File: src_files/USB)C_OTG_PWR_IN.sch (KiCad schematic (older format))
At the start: 19 parts, among them J10 Conn_01x02_Male, J11 USB_C_Receptacle

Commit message: updated footprint and schematics
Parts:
- removed J10: Conn_01x02_Male, Connector_Phoenix_MC:PhoenixContact_MC_1,5_2-G-3.81_1x02_P3.81mm_Horizontal, symbol Connector:Conn_01x02_Male
- added TP18: PWR_IN+, TestPoint:TestPoint_Pad_2.0x2.0mm, symbol Connector:TestPoint
- added TP19: PWR_IN-, TestPoint:TestPoint_Pad_2.0x2.0mm, symbol Connector:TestPoint
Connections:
- net GND: now also TP19.1
- net VBUS: now also TP18.1
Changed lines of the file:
@@
 $Descr A4 11693 8268
 encoding utf-8
-Sheet 14 15
+Sheet 13 16
 Title ""
 Date ""
@@
 Text HLabel 5875 2375 2    50   Input ~ 0
 USB_OTG0_VBUSDET
-$Comp
-L Connector:Conn_01x02_Male J10
-U 1 1 6A39320C
-P 1100 4950
-F 0 "J10" H 1208 5131 50  0000 C CNN
-F 1 "Conn_01x02_Male" H 1208 5040 50  0000 C CNN
-F 2 "Connector_Phoenix_MC:PhoenixContact_MC_1,5_2-G-3.81_1x02_P3.81mm_Horizontal" H 1100 4950 50  0001 C CNN
-F 3 "~" H 1100 4950 50  0001 C CNN
-	1    1100 4950
-	1    0    0    -1
-$EndComp
 Wire Wire Line
 	1300 4950 1825 4950
@@
 L OLIMEX_Power:GND #PWR?
 U 1 1 6A394CB4
-P 1800 5175
+P 1800 5300
 AR Path="/6A394CB4" Ref="#PWR?"  Part="1"
 AR Path="/6823D52E/6A394CB4" Ref="#PWR0267"  Part="1"
-F 0 "#PWR0267" H 1800 4925 50  0001 C CNN
-F 1 "GND" H 1805 5002 50  0000 C CNN
-F 2 "" H 1800 5175 60  0000 C CNN
-F 3 "" H 1800 5175 60  0000 C CNN
-	1    1800 5175
-	1    0    0    -1
-$EndComp
-Wire Wire Line
-	1300 5050 1800 5050
-Wire Wire Line
-	1800 5050 1800 5175
+F 0 "#PWR0267" H 1800 5050 50  0001 C CNN
+F 1 "GND" H 1805 5127 50  0000 C CNN
+F 2 "" H 1800 5300 60  0000 C CNN
+F 3 "" H 1800 5300 60  0000 C CNN
+	1    1800 5300
+	1    0    0    -1
+$EndComp
+Wire Wire Line
+	1300 5175 1800 5175
+Wire Wire Line
+	1800 5175 1800 5300
 Text Label 1825 4950 0    39   ~ 0
 POWER_IN_CONN
@@
 Wire Wire Line
 	7050 900  7275 900
+$Comp
+L Connector:TestPoint TP?
+U 1 1 62F91836
+P 1300 4950
+AR Path="/672F9255/62F91836" Ref="TP?"  Part="1"
+AR Path="/6823D52E/62F91836" Ref="TP18"  Part="1"
+F 0 "TP18" V 1254 5138 50  0000 L CNN
+F 1 "PWR_IN+" V 1345 5138 50  0000 L CNN
+F 2 "TestPoint:TestPoint_Pad_2.0x2.0mm" H 1500 4950 50  0001 C CNN
+F 3 "~" H 1500 4950 50  0001 C CNN
+	1    1300 4950
+	0    -1   -1   0
+$EndComp
+$Comp
+L Connector:TestPoint TP?
+U 1 1 62F9183C
+P 1300 5175
+AR Path="/672F9255/62F9183C" Ref="TP?"  Part="1"
+AR Path="/6823D52E/62F9183C" Ref="TP19"  Part="1"
+F 0 "TP19" V 1254 5363 50  0000 L CNN
+F 1 "PWR_IN-" V 1345 5363 50  0000 L CNN
+F 2 "TestPoint:TestPoint_Pad_2.0x2.0mm" H 1500 5175 50  0001 C CNN
+F 3 "~" H 1500 5175 50  0001 C CNN
+	1    1300 5175
+	0    -1   -1   0
+$EndComp
 $EndSCHEMATC

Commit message: wireless power TX RX added
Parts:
- removed D24: ESD5451R-2/TR, greencharge-footprints:DFP1006-2L, symbol Device:D_TVS
- removed F1: mSMD300, Fuse:Fuse_1812_4532Metric, symbol OLIMEX_Devices:FUSE
- removed J11: USB_C_Receptacle, greencharge-footprints:GCT_USB4056-03-A_REVA, symbol Connector:USB_C_Receptacle
- added C298, C306, C307: 10uF, Capacitor_SMD:C_0402_1005Metric, symbol Device:C_Small
- added C299: 4.7nF, Capacitor_SMD:C_0402_1005Metric, symbol Device:C_Small
- added C300, C301: 22nF, Capacitor_SMD:C_01005_0402Metric, symbol Device:C_Small
- added C302, C303, C304, C305, C313: 47nF, Capacitor_SMD:C_01005_0402Metric, symbol Device:C_Small
- added C308, C309: 2.2uF, Capacitor_SMD:C_0603_1608Metric, symbol Device:C_Small
- added C310, C311, C312: 10uF, Capacitor_SMD:C_0603_1608Metric, symbol Device:C_Small
- added C314, C315, C316: 100nF, Capacitor_SMD:C_01005_0402Metric, symbol Device:C_Small
- added C317: 15uF, Capacitor_SMD:C_0805_2012Metric, symbol Device:C_Small
- added C318, C319: 100nF, Capacitor_SMD:C_0402_1005Metric, symbol Device:C_Small
- added C320: 100pF, Capacitor_SMD:C_0402_1005Metric, symbol Device:C_Small
- added D4: LED, LED_SMD:LED_0603_1608Metric, symbol Device:LED
- added D5, D6: SMAJ16A, Diode_SMD:D_SMA, symbol dk_TVS-Diodes:ESD5Z3_3T1G
- added L16: MWSA1004S-3R3MT, greencharge-footprints:MWSA1004S-3R3MT, symbol OLIMEX_RCL:INDUCTOR_SMALL
- added R66, R67: 470R, Resistor_SMD:R_0402_1005Metric, symbol Device:R_US
- added R68, R69, R70: 47K, Resistor_SMD:R_0402_1005Metric, symbol Device:R_US
- added TP22: RX_COIL+, TestPoint:TestPoint_Pad_1.5x1.5mm, symbol Connector:TestPoint
- added TP23: rx_vout, TestPoint:TestPoint_Pad_2.0x2.0mm, symbol Connector:TestPoint
- added TP24: USB_D-, TestPoint:TestPoint_Pad_1.0x1.0mm, symbol Connector:TestPoint
- added TP25: USB_D+, TestPoint:TestPoint_Pad_1.0x1.0mm, symbol Connector:TestPoint
- added U13: STWLC68, greencharge-footprints:STWLC68, symbol GCL_Integrated-Circuits:STWLC68
- added U14: TPS56637RPAR, greencharge-footprints:TPS56637RPAR, symbol GCL_Integrated-Circuits:TPS56637RPAR
- R93: value 5.1K -> 100K
- R94: value 5.1K -> 20K
- R95: value 2.2R -> 73.2K
- R96: value 2.2R -> 10K
- TP16: value VBUS -> 5V_VIN
- TP17: value 5V -> RX_COIL-; footprint TestPoint:TestPoint_Pad_D1.0mm -> TestPoint:TestPoint_Pad_1.5x1.5mm
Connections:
- net +5V: now also R93.1, R94.1, R95.1, TP18.1, L16.2; no longer TP17.1
- net GND: now also R96.2, C298.2, C306.2, C307.2, C308.2, C309.2, C310.2, C311.2, C312.2, C317.2, C318.2, D5.A, D6.A, U13.A1 (VSSP), U13.A8 (VSSP), U13.B1 (VSSP), U13.B8 (VSSP), U13.C4 (VSSA), U13.C5 (VSSA), U13.D3 (VSSA), U13.D4 (VSSA), U13.E4 (VSSD), U13.E5 (VSSA), U13.F3 (VSSD), U13.F4 (VSSD), U13.F5 (VSSA), U13.F6 (VSSA), U13.G1 (DFT), U13.G2 (VSSD), U13.G3 (VSSD), U13.G4 (VSSD), U13.G6 (VSSA), U13.G7 (VSSA), U13.H3 (VSSD), U13.H4 (VSSD), U13.H5 (VSSD), U13.H6 (VSSD), U13.H7 (VSSD), U13.J5 (BOOT_SEL), U14.10 (MODE), U14.3 (AGND), U14.9 (PGND); no longer R93.1, R94.1
- net USB_OTG0_D+: now also TP25.1; no longer R96.1
- net USB_OTG0_D-: now also TP24.1; no longer R95.1
- net VBUS: no longer TP18.1
- net at R93.2: now also U14.4 (PG)
- net at R94.2: now also C320.2
- net at R95.2: now also R96.1, C320.1, U14.2 (FB)
- new net: C298.1, C299.2, C306.1, C307.1, R66.2, U13.A4 (VRECT), U13.A5 (VRECT), U13.B4 (VRECT), U13.B5 (VRECT), U13.C3 (VRECT)
- new net: C300.1, C302.1, C303.1, C313.2, C314.2, C315.2, C316.2, D5.K, U13.A6 (AC1), U13.A7 (AC1), U13.B6 (AC1), U13.B7 (AC1)
- new net: C304.2, U13.C1 (BOOT2)
- new net: R66.1, U13.C2 (IEXT)
- new net: U13.C6 (NC), U13.D6 (NC)
- new net: C305.2, U13.C7 (CLAMP2)
- new net: C302.2, U13.C8 (CLAMP1)
- new net: C301.2, U13.D7 (COMM2)
- new net: C300.2, U13.D8 (COMM1)
- new net: C308.1, U13.E6 (V5V0), U13.F7 (V5V0)
- new net: C303.2, U13.E7 (BOOT1)
- new net: C299.1, U13.E8 (BOOT)
- new net: D4.1 (K), U13.H2 (GPIO0)
- new net: R69.2, U13.H8 (SCL)
- new net: R68.2, U13.J7 (INTB)
- new net: R70.2, U13.J8 (SDA)
- new net: D4.2 (A), R67.2
- new net: C319.2, L16.1, U14.6 (SW)
- new net: C319.1, U14.7 (BOOT)
- new net COIL+: C313.1, C314.1, C315.1, C316.1, TP22.1
- new net COIL-: C301.1, C304.1, C305.1, D6.K, TP17.1, U13.A2 (AC2), U13.A3 (AC2), U13.B2 (AC2), U13.B3 (AC2)
- new net RX_VOUT: C310.1, C311.1, C312.1, C317.1, C318.1, TP23.1, U13.D2 (VOUT), U13.E1 (VOUT), U13.E2 (VOUT), U13.E3 (VOUT), U13.F2 (VOUT), U14.1 (EN), U14.11 (VIN_2), U14.12 (VIN_3), U14.13 (VIN_4), U14.8 (VIN_1)
- new net v1v8: C309.1, R67.1, R68.1, R69.1, R70.1, U13.G5 (V1V8), U13.G8 (V1V8), U13.J6 (RSTB)
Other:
- note added: "5V 6A BUCK"
- note added: "FILTER"
- note added: "MAIN SYSTEM SUPPLY RAIL\n5V / 6A"
- note added: "OPTIONAL POWER INPUT 5V >2A"
- note added: "PROGRAMABLE OUTPUT OF THE \nRECEIVER LDO RANGE 2.5W-20W. \nso MAX OUT= 20V at 1A."
- note added: "WIRELESS POWER RECEIVER"
- note added: "base on selection\nto achieve 100KHz resonance\nL=7.3uH C=350nF"
- note added: "coil type A5\nhttps://kimchen8.en.made-in-china.com/product/uBcmjaAlYKht/China-Square-Rx-Coil-Antenna-Coil-for-Samsung-Charging-Receiver.html"
- note added: "to filter out V_spikes"
- moved on the sheet: C254, C255, C256, C257, C258, D23, D25, R97, R98, TP16, TP18, TP19

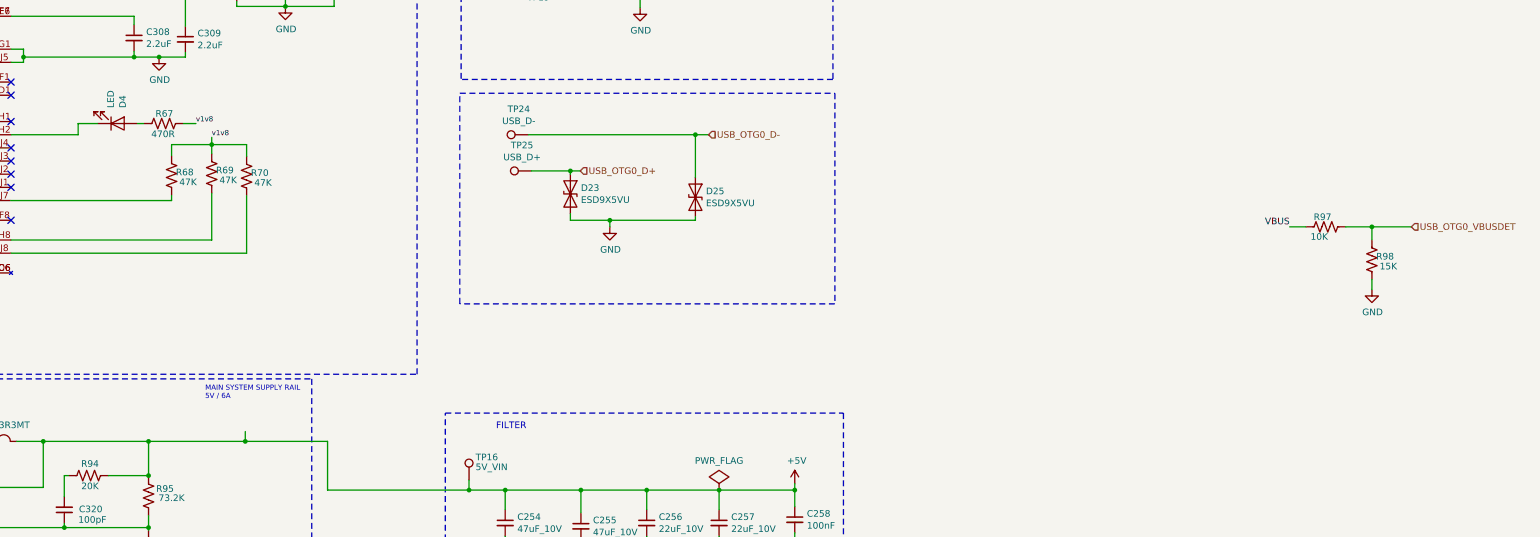
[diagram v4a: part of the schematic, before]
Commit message: updates rules check and associations
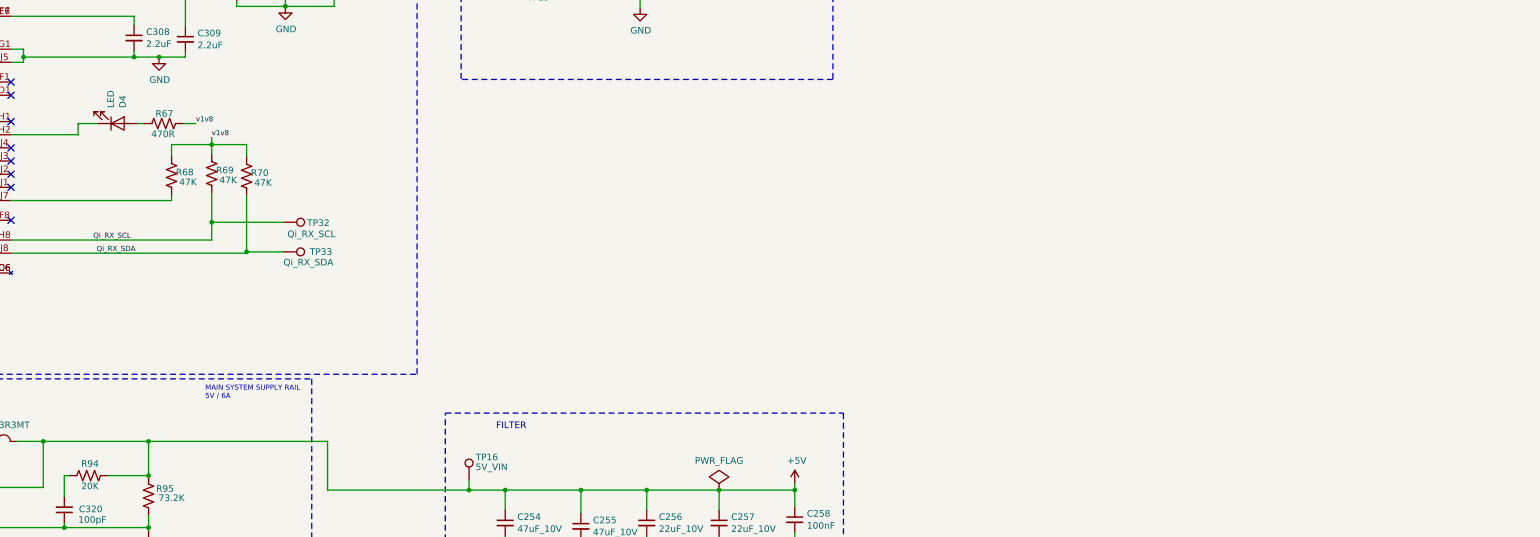
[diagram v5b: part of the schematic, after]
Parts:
- removed D23, D25: ESD9X5VU, greencharge-footprints:ESD9X5VU_DFN1006-2, symbol Device:D_TVS
- removed R97: 10K, Resistor_SMD:R_0402_1005Metric, symbol Device:R_US
- removed R98: 15K, Resistor_SMD:R_0402_1005Metric, symbol Device:R_US
- removed TP24: USB_D-, TestPoint:TestPoint_Pad_1.0x1.0mm, symbol Connector:TestPoint
- removed TP25: USB_D+, TestPoint:TestPoint_Pad_1.0x1.0mm, symbol Connector:TestPoint
- added TP32: Qi_RX_SCL, TestPoint:TestPoint_Pad_D1.0mm, symbol Connector:TestPoint
- added TP33: Qi_RX_SDA, TestPoint:TestPoint_Pad_D1.0mm, symbol Connector:TestPoint
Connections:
- net Qi_RX_SCL: now reaches R69.2, U13.H8 (SCL)
- net Qi_RX_SCL: now also TP32.1
- net Qi_RX_SDA: now reaches R70.2, U13.J8 (SDA)
- net Qi_RX_SDA: now also TP33.1
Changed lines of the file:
@@
 $Descr A4 11693 8268
 encoding utf-8
-Sheet 11 17
+Sheet 17 17
 Title ""
 Date ""
@@
 $EndDescr
 $Comp
-L Device:D_TVS D?
-U 1 1 682BBBF7
-P 8990 2755
-AR Path="/61C73AB6/682BBBF7" Ref="D?"  Part="1"
-AR Path="/682BBBF7" Ref="D?"  Part="1"
-AR Path="/6823D52E/682BBBF7" Ref="D23"  Part="1"
-F 0 "D23" V 8944 2835 50  0000 L CNN
-F 1 "ESD9X5VU" V 9035 2835 50  0000 L CNN
-F 2 "greencharge-footprints:ESD9X5VU_DFN1006-2" H 8990 2755 50  0001 C CNN
-F 3 "~" H 8990 2755 50  0001 C CNN
-	1    8990 2755
-	0    1    1    0
-$EndComp
-$Comp
 L Device:C_Small C?
 U 1 1 682BBC5C
@@
 	1    0    0    -1
 $EndComp
-$Comp
-L OLIMEX_Power:GND #PWR?
-U 1 1 682BBC7A
-P 9290 3005
-AR Path="/682BBC7A" Ref="#PWR?"  Part="1"
-AR Path="/6823D52E/682BBC7A" Ref="#PWR0271"  Part="1"
-F 0 "#PWR0271" H 9290 2755 50  0001 C CNN
-F 1 "GND" H 9295 2832 50  0000 C CNN
-F 2 "" H 9290 3005 60  0000 C CNN
-F 3 "" H 9290 3005 60  0000 C CNN
-	1    9290 3005
-	1    0    0    -1
-$EndComp
-Wire Wire Line
-	8990 2905 8990 2955
-Wire Wire Line
-	8990 2955 9290 2955
-Wire Wire Line
-	9290 2955 9290 3005
-Connection ~ 9290 2955
 Wire Wire Line
 	10695 5005 10695 5130
@@
 Wire Wire Line
 	9520 1215 9520 1340
-Wire Wire Line
-	8990 2580 8990 2605
-Text HLabel 9065 2580 2    50   Input ~ 0
-USB_OTG0_D+
-Text HLabel 10040 2305 2    50   Input ~ 0
-USB_OTG0_D-
-Wire Wire Line
-	9940 2955 9940 2930
-Wire Wire Line
-	9290 2955 9940 2955
-$Comp
-L Device:D_TVS D?
-U 1 1 682BBC24
-P 9940 2780
-AR Path="/61C73AB6/682BBC24" Ref="D?"  Part="1"
-AR Path="/682BBC24" Ref="D?"  Part="1"
-AR Path="/6823D52E/682BBC24" Ref="D25"  Part="1"
-F 0 "D25" V 9894 2860 50  0000 L CNN
-F 1 "ESD9X5VU" V 9985 2860 50  0000 L CNN
-F 2 "greencharge-footprints:ESD9X5VU_DFN1006-2" H 9940 2780 50  0001 C CNN
-F 3 "~" H 9940 2780 50  0001 C CNN
-	1    9940 2780
-	0    1    1    0
-$EndComp
-Wire Wire Line
-	9065 2580 8990 2580
-Wire Wire Line
-	10040 2305 9940 2305
 $Comp
 L OLIMEX_Power:PWR_FLAG #FLG0101
@@
 	4740 3105 6265 3105
 Wire Wire Line
-	6265 3105 6265 2750
-Wire Wire Line
-	4740 3205 6530 3205
-Wire Wire Line
-	6530 3205 6530 2770
+	6265 3105 6265 2970
 Wire Wire Line
 	4740 2805 5960 2805
@@
 	1    0    0    -1
 $EndComp
-$Comp
-L Connector:TestPoint TP24
-U 1 1 622DC098
-P 8670 2305
-F 0 "TP24" V 8865 2377 50  0000 C CNN
-F 1 "USB_D-" V 8774 2377 50  0000 C CNN
-F 2 "TestPoint:TestPoint_Pad_1.0x1.0mm" H 8870 2305 50  0001 C CNN
-F 3 "~" H 8870 2305 50  0001 C CNN
-	1    8670 2305
-	0    -1   -1   0
-$EndComp
-$Comp
-L Connector:TestPoint TP25
-U 1 1 6230EBE6
-P 8695 2580
-F 0 "TP25" V 8890 2652 50  0000 C CNN
-F 1 "USB_D+" V 8799 2652 50  0000 C CNN
-F 2 "TestPoint:TestPoint_Pad_1.0x1.0mm" H 8895 2580 50  0001 C CNN
-F 3 "~" H 8895 2580 50  0001 C CNN
-	1    8695 2580
-	0    -1   -1   0
-$EndComp
-Wire Wire Line
-	8990 2580 8695 2580
-Connection ~ 8990 2580
-Wire Wire Line
-	8670 2305 9940 2305
-Connection ~ 9940 2305
-Wire Wire Line
-	9940 2305 9940 2630
-Text Label 14455 3005 2    50   ~ 0
-VBUS
-Wire Wire Line
-	14455 3005 14580 3005
-$Comp
-L OLIMEX_Power:GND #PWR?
-U 1 1 682BBC41
-P 15080 3480
-AR Path="/682BBC41" Ref="#PWR?"  Part="1"
-AR Path="/6823D52E/682BBC41" Ref="#PWR0272"  Part="1"
-F 0 "#PWR0272" H 15080 3230 50  0001 C CNN
-F 1 "GND" H 15085 3307 50  0000 C CNN
-F 2 "" H 15080 3480 60  0000 C CNN
-F 3 "" H 15080 3480 60  0000 C CNN
-	1    15080 3480
-	1    0    0    -1
-$EndComp
-Text HLabel 15380 3005 2    50   Input ~ 0
-USB_OTG0_VBUSDET
-Wire Wire Line
-	15080 3480 15080 3405
-Wire Wire Line
-	15080 3005 15380 3005
-Wire Wire Line
-	14880 3005 15080 3005
-Connection ~ 15080 3005
-Wire Wire Line
-	15080 3005 15080 3105
-$Comp
-L Device:R_US R?
-U 1 1 682BBC37
-P 15080 3255
-AR Path="/682BBC37" Ref="R?"  Part="1"
-AR Path="/6823D52E/682BBC37" Ref="R98"  Part="1"
-F 0 "R98" H 15180 3280 50  0000 C CNN
-F 1 "15K" H 15205 3205 50  0000 C CNN
-F 2 "Resistor_SMD:R_0402_1005Metric" V 15120 3245 50  0001 C CNN
-F 3 "~" H 15080 3255 50  0001 C CNN
-	1    15080 3255
-	1    0    0    -1
-$EndComp
-$Comp
-L Device:R_US R?
-U 1 1 682BBC31
-P 14730 3005
-AR Path="/682BBC31" Ref="R?"  Part="1"
-AR Path="/6823D52E/682BBC31" Ref="R97"  Part="1"
-F 0 "R97" V 14655 2980 50  0000 C CNN
-F 1 "10K" V 14805 2955 50  0000 C CNN
-F 2 "Resistor_SMD:R_0402_1005Metric" V 14770 2995 50  0001 C CNN
-F 3 "~" H 14730 3005 50  0001 C CNN
-	1    14730 3005
-	0    1    1    0
-$EndComp
 Text Notes 6295 875  0    39   ~ 0
 PROGRAMABLE OUTPUT OF THE \nRECEIVER LDO RANGE 2.5W-20W. \nso MAX OUT= 20V at 1A.
@@
 Connection ~ 5145 5290
 Connection ~ 5785 4635
-Wire Wire Line
-	6520 4560 6520 4635
 Text Notes 6215 4320 0    39   ~ 0
 MAIN SYSTEM SUPPLY RAIL\n5V / 6A
@@
 Wire Wire Line
 	7145 5005 8220 5005
-Wire Wire Line
-	5785 4635 6520 4635
-Connection ~ 6520 4635
-Wire Wire Line
-	6520 4635 7145 4635
 Connection ~ 8220 5005
 Wire Wire Line
@@
 	8040 4420 11065 4420
 Wire Notes Line
-	11000 1990 11000 3590
-Wire Notes Line
-	11000 3590 8150 3590
-Wire Notes Line
-	8150 3590 8150 1990
-Wire Notes Line
-	8150 1990 11000 1990
-Wire Notes Line
 	8165 595  10985 595
 Wire Notes Line
@@
 Wire Wire Line
 	9020 990  9545 990
+Wire Wire Line
+	5785 4635 7145 4635
+Text Label 5365 3105 0    39   ~ 0
+Qi_RX_SCL
+Text Label 5390 3205 0    39   ~ 0
+Qi_RX_SDA
+$Comp
+L Connector:TestPoint TP?
+U 1 1 640203A8
+P 6810 2970
+AR Path="/61C73AB6/640203A8" Ref="TP?"  Part="1"
+AR Path="/62F6D336/640203A8" Ref="TP?"  Part="1"
+AR Path="/6823D52E/640203A8" Ref="TP32"  Part="1"
+F 0 "TP32" V 6815 3150 50  0000 L CNN
+F 1 "Qi_RX_SCL" V 6900 3000 50  0000 L CNN
+F 2 "TestPoint:TestPoint_Pad_D1.0mm" H 7010 2970 50  0001 C CNN
+F 3 "~" H 7010 2970 50  0001 C CNN
+	1    6810 2970
+	0    1    1    0
+$EndComp
+Wire Wire Line
+	4740 3205 6530 3205
+Connection ~ 6530 3195
+Wire Wire Line
+	6530 3195 6530 2770
+Wire Wire Line
+	6530 3205 6530 3195
+Wire Wire Line
+	6810 3195 6530 3195
+$Comp
+L Connector:TestPoint TP?
+U 1 1 6403E2AC
+P 6810 3195
+AR Path="/61C73AB6/6403E2AC" Ref="TP?"  Part="1"
+AR Path="/62F6D336/6403E2AC" Ref="TP?"  Part="1"
+AR Path="/6823D52E/6403E2AC" Ref="TP33"  Part="1"
+F 0 "TP33" V 6810 3395 50  0000 L CNN
+F 1 "Qi_RX_SDA" V 6890 3195 50  0000 L CNN
+F 2 "TestPoint:TestPoint_Pad_D1.0mm" H 7010 3195 50  0001 C CNN
+F 3 "~" H 7010 3195 50  0001 C CNN
+	1    6810 3195
+	0    1    1    0
+$EndComp
+Wire Wire Line
+	6810 2970 6265 2970
+Connection ~ 6265 2970
+Wire Wire Line
+	6265 2970 6265 2750
 $EndSCHEMATC

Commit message: layout change
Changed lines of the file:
@@
 AR Path="/626A6204/62FDE5CD" Ref="TP?"  Part="1"
 AR Path="/6823D52E/62FDE5CD" Ref="TP22"  Part="1"
-F 0 "TP22" V 869 1858 50  0000 L CNN
+F 0 "TP22" V 860 1820 50  0000 L CNN
 F 1 "RX_COIL+" V 995 1610 50  0000 L CNN
 F 2 "TestPoint:TestPoint_Pad_1.5x1.5mm" H 1115 1670 50  0001 C CNN
@@
 AR Path="/626A6204/62FDE5D4" Ref="TP?"  Part="1"
 AR Path="/6823D52E/62FDE5D4" Ref="TP17"  Part="1"
-F 0 "TP17" V 844 2133 50  0000 L CNN
+F 0 "TP17" V 815 2070 50  0000 L CNN
 F 1 "RX_COIL-" V 955 1835 50  0000 L CNN
 F 2 "TestPoint:TestPoint_Pad_1.5x1.5mm" H 1090 1945 50  0001 C CNN
